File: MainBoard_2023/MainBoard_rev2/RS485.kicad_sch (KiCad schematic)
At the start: 8 parts, among them U14 LTC1480CN8#PBF

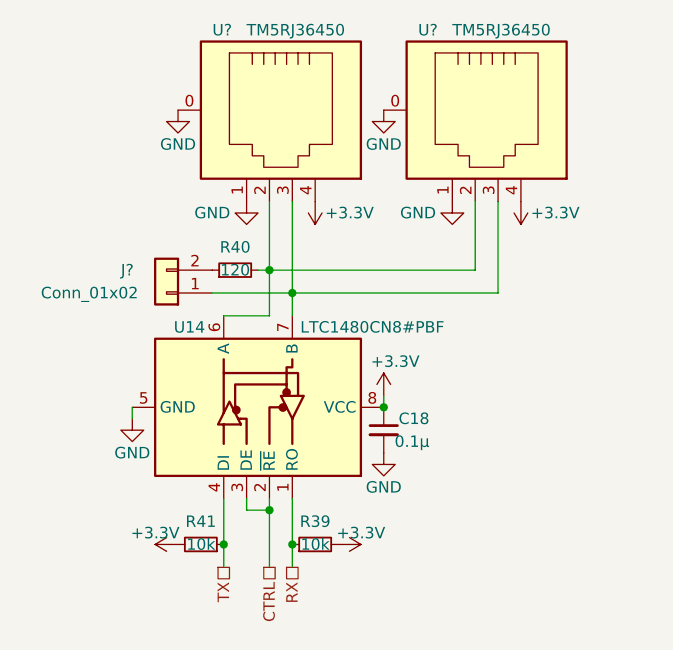
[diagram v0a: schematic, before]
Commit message: PCBファイルを作成
3Dモデルを割り当て　ブロックタイプエミフィルのパッドを小さくした
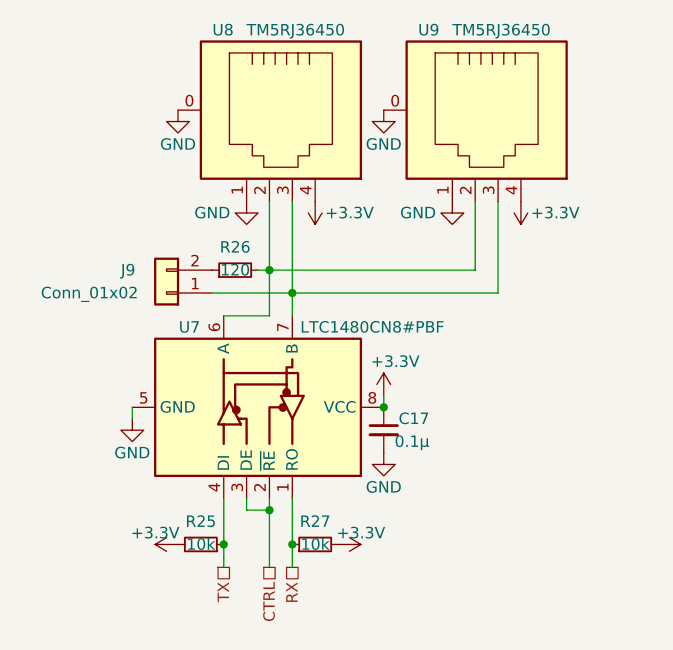
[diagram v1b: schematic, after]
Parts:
- J9: renamed from J?; footprint (none) -> Connector_PinHeader_2.54mm:PinHeader_1x02_P2.54mm_Vertical
- U8, U9: renamed from U?; footprint (none) -> TM5RJ36450:TM5RJ36450
- renumbered C18 to C17, R41 to R25, R40 to R26, R39 to R27, U14 to U7
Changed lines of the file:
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@@
   (symbol (lib_id "power:GND") (at 209.55 101.6 0) (mirror y) (unit 1)
     (in_bom yes) (on_board yes)
-    (property "Reference" "#PWR?" (id 0) (at 209.55 107.95 0)
+    (property "Reference" "#PWR073" (id 0) (at 209.55 107.95 0)
       (effects (font (size 1.27 1.27)) hide)
     )
@@
   (symbol (lib_id "power:GND") (at 209.55 63.5 0) (unit 1)
     (in_bom yes) (on_board yes)
-    (property "Reference" "#PWR?" (id 0) (at 209.55 69.85 0)
+    (property "Reference" "#PWR071" (id 0) (at 209.55 69.85 0)
       (effects (font (size 1.27 1.27)) hide)
     )
@@
   (symbol (lib_id "Interface_UART:MAX485E") (at 196.85 96.52 270) (mirror x) (unit 1)
     (in_bom yes) (on_board yes)
-    (property "Reference" "U14" (id 0) (at 187.96 87.63 90))
+    (property "Reference" "U7" (id 0) (at 187.96 87.63 90))
     (property "Value" "LTC1480CN8#PBF" (id 1) (at 208.28 87.63 90))
     (property "Footprint" "Package_DIP:DIP-8_W7.62mm_LongPads" (id 2) (at 179.07 96.52 0)
@@
   (symbol (lib_id "Device:R_Small") (at 193.04 81.28 90) (unit 1)
     (in_bom yes) (on_board yes)
-    (property "Reference" "R40" (id 0) (at 193.04 78.74 90))
+    (property "Reference" "R26" (id 0) (at 193.04 78.74 90))
     (property "Value" "120" (id 1) (at 193.04 81.28 90))
     (property "Footprint" "Resistor_SMD:R_0603_1608Metric_Pad0.98x0.95mm_HandSolder" (id 2) (at 193.04 81.28 0)
@@
   (symbol (lib_id "TM5RJ36450:TM5RJ36450") (at 220.98 63.5 270) (unit 1)
     (in_bom yes) (on_board yes)
-    (property "Reference" "U?" (id 0) (at 213.36 54.61 90)
+    (property "Reference" "U9" (id 0) (at 213.36 54.61 90)
       (effects (font (size 1.27 1.27)) (justify left))
     )
@@
       (effects (font (size 1.27 1.27)) (justify left))
     )
-    (property "Footprint" "" (id 2) (at 231.14 63.5 0)
+    (property "Footprint" "TM5RJ36450:TM5RJ36450" (id 2) (at 231.14 63.5 0)
       (effects (font (size 1.27 1.27)) hide)
     )
@@
   (symbol (lib_id "power:GND") (at 186.69 63.5 0) (unit 1)
     (in_bom yes) (on_board yes)
-    (property "Reference" "#PWR?" (id 0) (at 186.69 69.85 0)
+    (property "Reference" "#PWR066" (id 0) (at 186.69 69.85 0)
       (effects (font (size 1.27 1.27)) hide)
     )
@@
   (symbol (lib_id "power:GND") (at 181.61 97.79 0) (mirror y) (unit 1)
     (in_bom yes) (on_board yes)
-    (property "Reference" "#PWR0118" (id 0) (at 181.61 104.14 0)
+    (property "Reference" "#PWR065" (id 0) (at 181.61 104.14 0)
       (effects (font (size 1.27 1.27)) hide)
     )
@@
   (symbol (lib_id "power:GND") (at 217.17 73.66 0) (unit 1)
     (in_bom yes) (on_board yes)
-    (property "Reference" "#PWR0115" (id 0) (at 217.17 80.01 0)
+    (property "Reference" "#PWR074" (id 0) (at 217.17 80.01 0)
       (effects (font (size 1.27 1.27)) hide)
     )
@@
   (symbol (lib_id "power:+3.3V") (at 209.55 95.25 0) (mirror y) (unit 1)
     (in_bom yes) (on_board yes)
-    (property "Reference" "#PWR0109" (id 0) (at 209.55 99.06 0)
+    (property "Reference" "#PWR072" (id 0) (at 209.55 99.06 0)
       (effects (font (size 1.27 1.27)) hide)
     )
@@
   (symbol (lib_id "Device:R_Small") (at 189.23 111.76 270) (mirror x) (unit 1)
     (in_bom yes) (on_board yes)
-    (property "Reference" "R41" (id 0) (at 189.23 109.22 90))
+    (property "Reference" "R25" (id 0) (at 189.23 109.22 90))
     (property "Value" "10k" (id 1) (at 189.23 111.76 90))
     (property "Footprint" "Resistor_SMD:R_0603_1608Metric_Pad0.98x0.95mm_HandSolder" (id 2) (at 189.23 111.76 0)
@@
   (symbol (lib_id "Connector_Generic:Conn_01x02") (at 185.42 83.82 180) (unit 1)
     (in_bom yes) (on_board yes)
-    (property "Reference" "J?" (id 0) (at 180.34 81.28 0)
+    (property "Reference" "J9" (id 0) (at 180.34 81.28 0)
       (effects (font (size 1.27 1.27)) (justify right))
     )
@@
       (effects (font (size 1.27 1.27)) (justify right))
     )
-    (property "Footprint" "" (id 2) (at 185.42 83.82 0)
+    (property "Footprint" "Connector_PinHeader_2.54mm:PinHeader_1x02_P2.54mm_Vertical" (id 2) (at 185.42 83.82 0)
       (effects (font (size 1.27 1.27)) hide)
     )
@@
   (symbol (lib_id "Device:C_Small") (at 209.55 99.06 0) (mirror y) (unit 1)
     (in_bom yes) (on_board yes)
-    (property "Reference" "C18" (id 0) (at 214.63 97.79 0)
+    (property "Reference" "C17" (id 0) (at 214.63 97.79 0)
       (effects (font (size 1.27 1.27)) (justify left))
     )
@@
   (symbol (lib_id "TM5RJ36450:TM5RJ36450") (at 198.12 63.5 270) (unit 1)
     (in_bom yes) (on_board yes)
-    (property "Reference" "U?" (id 0) (at 190.5 54.61 90)
+    (property "Reference" "U8" (id 0) (at 190.5 54.61 90)
       (effects (font (size 1.27 1.27)) (justify left))
     )
@@
       (effects (font (size 1.27 1.27)) (justify left))
     )
-    (property "Footprint" "" (id 2) (at 208.28 63.5 0)
+    (property "Footprint" "TM5RJ36450:TM5RJ36450" (id 2) (at 208.28 63.5 0)
       (effects (font (size 1.27 1.27)) hide)
     )
@@
   (symbol (lib_id "power:+3.3V") (at 204.47 111.76 270) (unit 1)
     (in_bom yes) (on_board yes)
-    (property "Reference" "#PWR0111" (id 0) (at 200.66 111.76 0)
+    (property "Reference" "#PWR070" (id 0) (at 200.66 111.76 0)
       (effects (font (size 1.27 1.27)) hide)
     )
@@
   (symbol (lib_id "power:+3.3V") (at 186.69 111.76 90) (mirror x) (unit 1)
     (in_bom yes) (on_board yes)
-    (property "Reference" "#PWR0116" (id 0) (at 190.5 111.76 0)
+    (property "Reference" "#PWR067" (id 0) (at 190.5 111.76 0)
       (effects (font (size 1.27 1.27)) hide)
     )
@@
   (symbol (lib_id "power:+3.3V") (at 201.93 73.66 180) (unit 1)
     (in_bom yes) (on_board yes)
-    (property "Reference" "#PWR0112" (id 0) (at 201.93 69.85 0)
+    (property "Reference" "#PWR069" (id 0) (at 201.93 69.85 0)
       (effects (font (size 1.27 1.27)) hide)
     )
@@
   (symbol (lib_id "power:+3.3V") (at 224.79 73.66 180) (unit 1)
     (in_bom yes) (on_board yes)
-    (property "Reference" "#PWR0117" (id 0) (at 224.79 69.85 0)
+    (property "Reference" "#PWR075" (id 0) (at 224.79 69.85 0)
       (effects (font (size 1.27 1.27)) hide)
     )
@@
   (symbol (lib_id "Device:R_Small") (at 201.93 111.76 90) (unit 1)
     (in_bom yes) (on_board yes)
-    (property "Reference" "R39" (id 0) (at 201.93 109.22 90))
+    (property "Reference" "R27" (id 0) (at 201.93 109.22 90))
     (property "Value" "10k" (id 1) (at 201.93 111.76 90))
     (property "Footprint" "Resistor_SMD:R_0603_1608Metric_Pad0.98x0.95mm_HandSolder" (id 2) (at 201.93 111.76 0)
@@
   (symbol (lib_id "power:GND") (at 194.31 73.66 0) (unit 1)
     (in_bom yes) (on_board yes)
-    (property "Reference" "#PWR0110" (id 0) (at 194.31 80.01 0)
-      (effects (font (size 1.27 1.27)) hide)
-    )
+    (property "Reference" "#PWR068" (id 0) (at 194.31 80.01 0)
+      (effects (font (size 1.27 1.27)) hide)
+    )

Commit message: メイン基板配置中
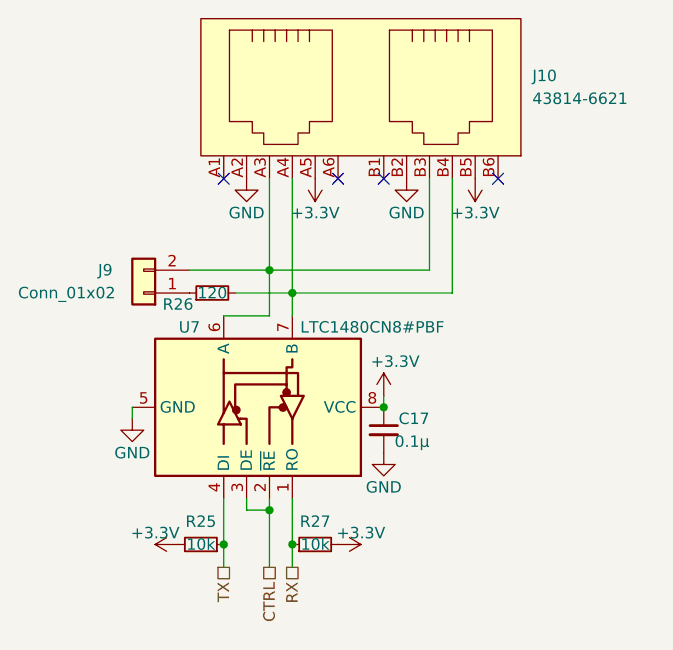
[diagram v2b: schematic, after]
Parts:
- removed U8, U9: TM5RJ36450, TM5RJ36450:TM5RJ36450, symbol TM5RJ36450:TM5RJ36450
- added J10: 43814-6621, Molex_6P6C_Right_Angle_TH_RJ11_Modular_Jack_Connector:Molex_6P6C_Right_Angle_TH_RJ11_Modular_Jack_Connector, symbol Molex_6P6C_Right_Angle_TH_RJ11_Modular_Jack_Connector:43814-6621
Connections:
- net +3.3V: now also J10.A5, J10.B5
- net GND: now also J10.A2, J10.B2
- net at U7.6 (A): now also J9.2 (Pin_2), J10.A3, J10.B3; no longer R26.2
- net at U7.7 (B): now also R26.2, J10.A4, J10.B4; no longer J9.1 (Pin_1)
- net at R26.1: now also J9.1 (Pin_1); no longer J9.2 (Pin_2)
- no-connect marks 0 -> 4
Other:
- moved on the sheet: J9, R26
